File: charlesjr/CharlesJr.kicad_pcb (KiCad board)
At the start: 2 copper layers, 10 parts, among them P1 CONN_01X03

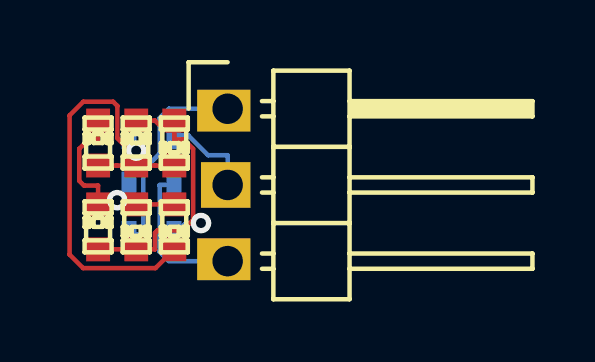
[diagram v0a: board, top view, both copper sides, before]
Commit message: Upload rev2.
Improved silkscreen, higher track width for header to resistor
connections, add "rev2" text.
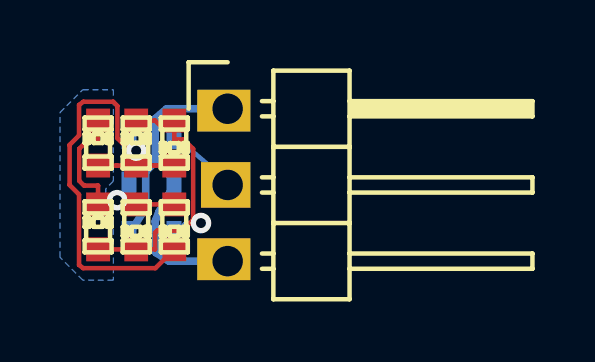
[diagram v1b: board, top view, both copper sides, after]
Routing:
- added copper zone on B.Cu, net (none)
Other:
- net class Thicker added: clearance 0.1524, trace_width 0.254, via_dia 0.6858, via_drill 0.3302
- board text added: "/"
- board text added: "cc0"
- board text added: "charles"
- board text added: "made"
- board text added: "rev2"
